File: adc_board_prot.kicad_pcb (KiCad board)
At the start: 6 copper layers, 146 x 138.7 mm, 331 parts, among them J1 USB4105-GF-A, J2 TMJG4820GENL, J3 5747841-4, J4 5747841-4, SW1 SDA02H1SBDR, SW2 FSM6JSMATR, U1 ADA4945-1, U10 LT3579, U11 LT3093, U12 LT8624S, U13 LT3045, U14 LT3045, U15 LT3045, U16 LT3045, U17 ADA4945-1, U18 LTC2387-18, U19 ADA4945-1, U2 LTC2387-18, U20 LTC2387-18, U21 ADA4945-1, U22 LTC2387-18, U23 24LC16BT-I/OT, U3 93AA56BT-I/OT, U4 FT2232HL, U5 TVS1800DRV, U6 TPS259480AYWPR, U7 LT8642S, U8 LT8350S, U9 LT3042, X1 ECS-2520MVLC-120-CN-TR

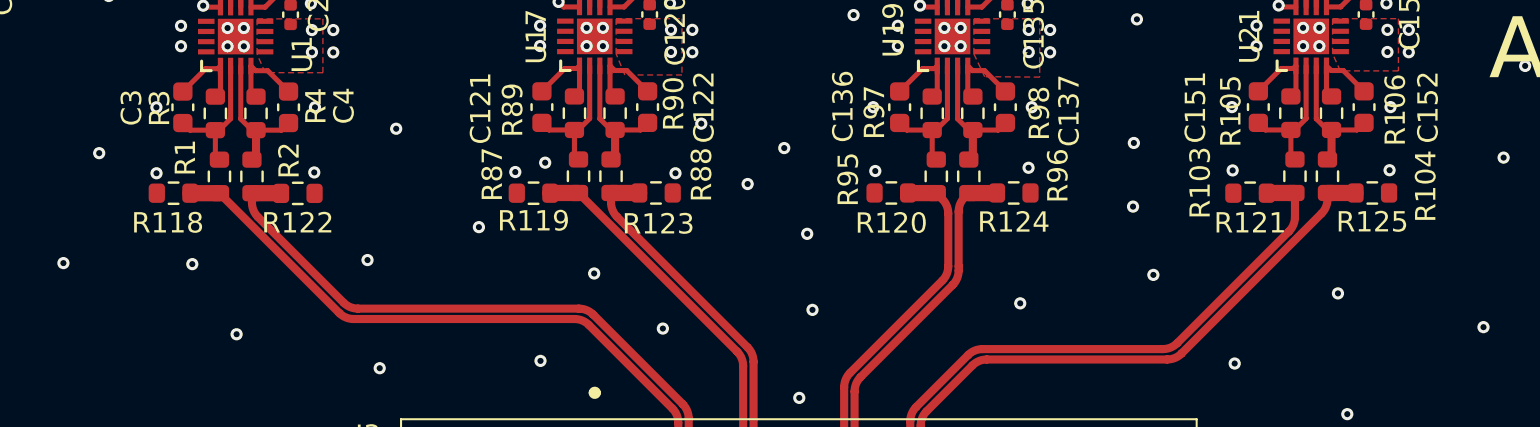
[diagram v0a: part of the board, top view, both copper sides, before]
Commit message: Remove floating resistor and reorder schematic pages
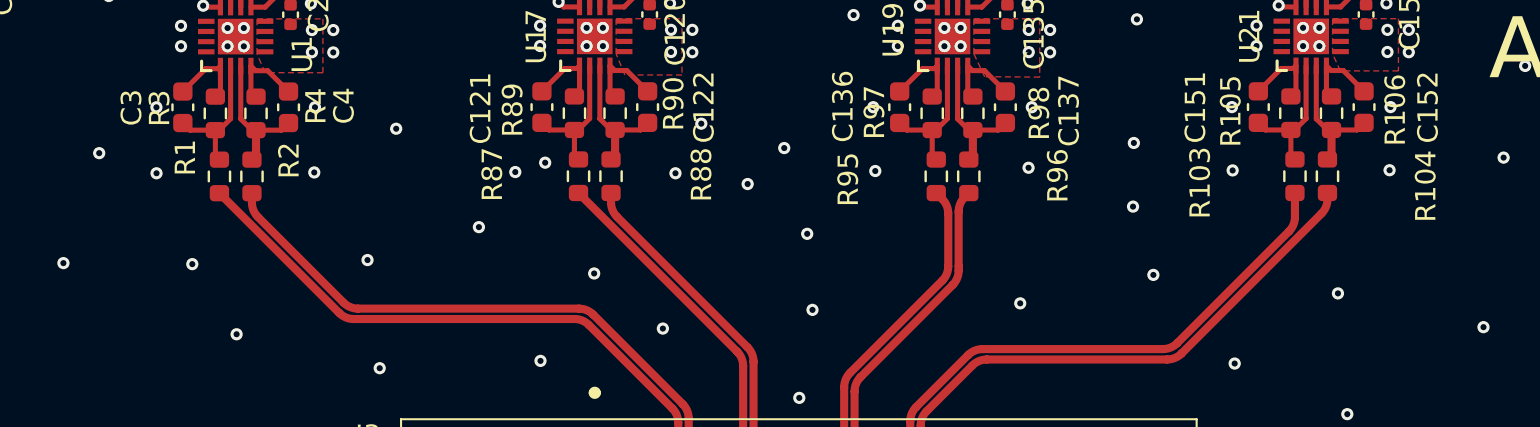
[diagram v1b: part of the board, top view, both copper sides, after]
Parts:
- removed R118, R119, R120, R121, R122, R123, R124, R125: 100k, Resistor_SMD:R_0603_1608Metric
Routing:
- net IN0+: track 33.0 -> 31.5 mm
- net IN0-: track 30.9 -> 29.5 mm
- net IN1-: track 20.7 -> 19.3 mm
- net IN2-: track 17.0 -> 15.7 mm
- net IN2+: track 19.5 -> 18.1 mm
- net IN1+: track 17.6 -> 16.2 mm
- net IN3-: track 30.7 -> 29.3 mm
- net IN3+: track 28.6 -> 27.2 mm
